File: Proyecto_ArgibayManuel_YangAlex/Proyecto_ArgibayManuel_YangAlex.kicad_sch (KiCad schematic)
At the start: 30 parts, among them J1 Conn_01x02, J2 Conn_01x01, J3 Con_1x2, J4 Con_1x3, J5 Conn_01x03_Pin, J6 Conn_01x07, SW1 SW_Push, SW2 SW_Push, SW3 SW_Push, SW4 SW_Push, U1 PIC18F258-I_SO, U2 HDC2010YPAR, U3 LT1716IS5TRMPBF, U4 LT1716IS5TRMPBF, U5 TXS0108EPW, Y1 Crystal

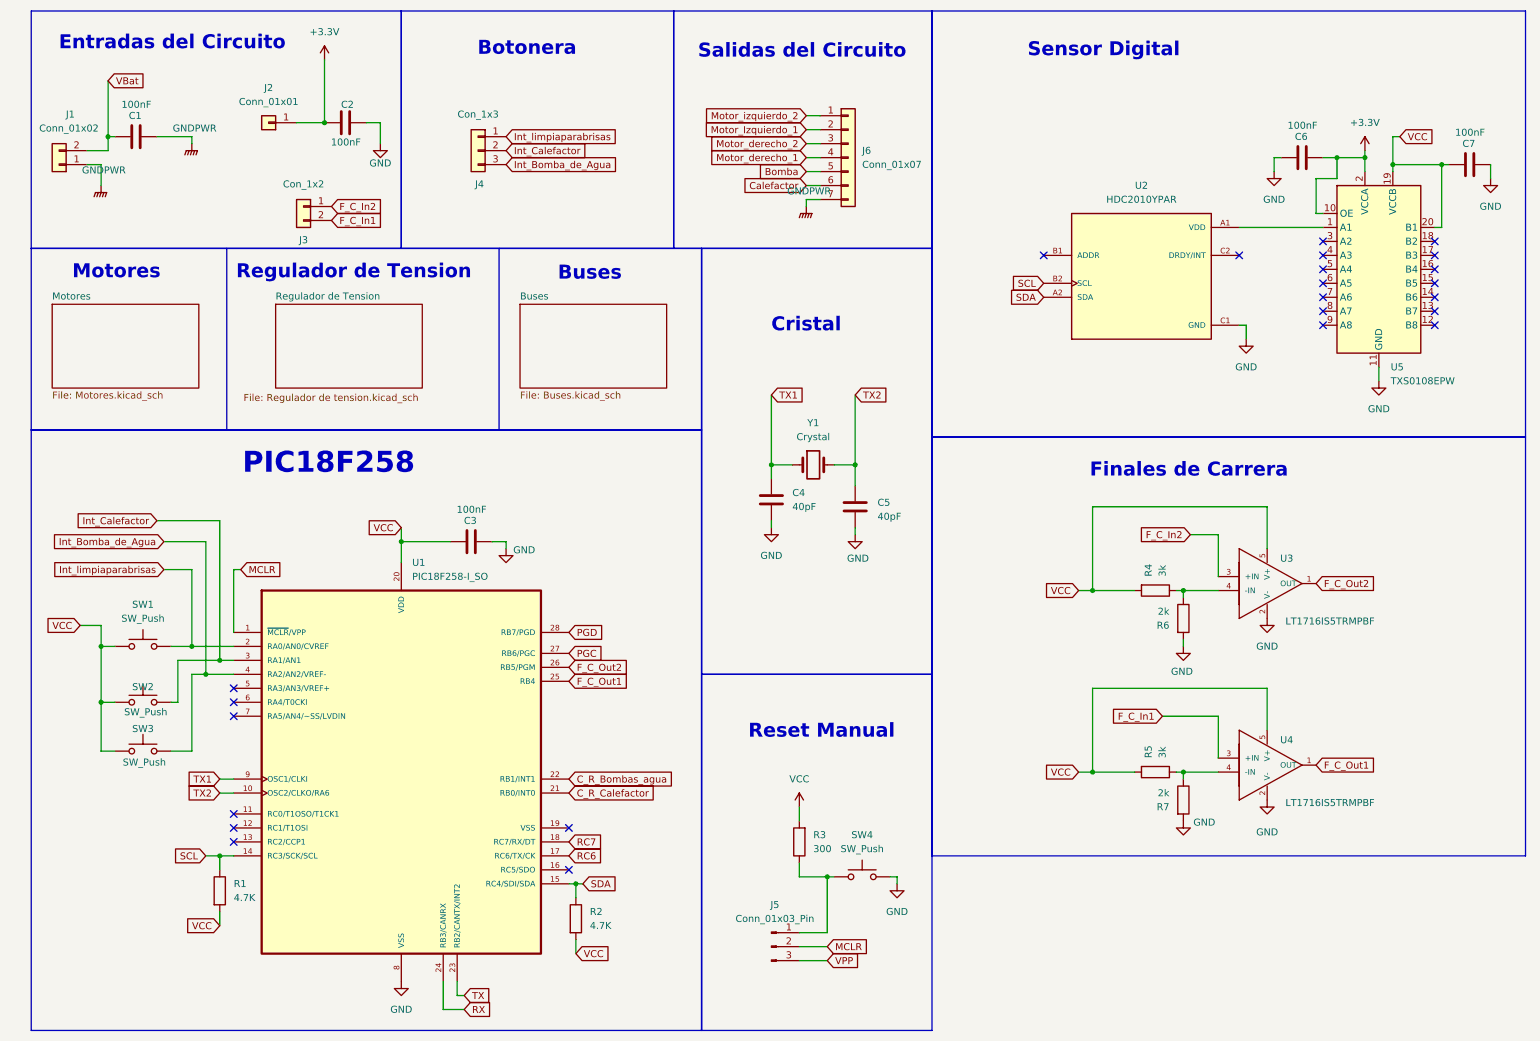
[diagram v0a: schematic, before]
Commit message: Separacion de Botonera
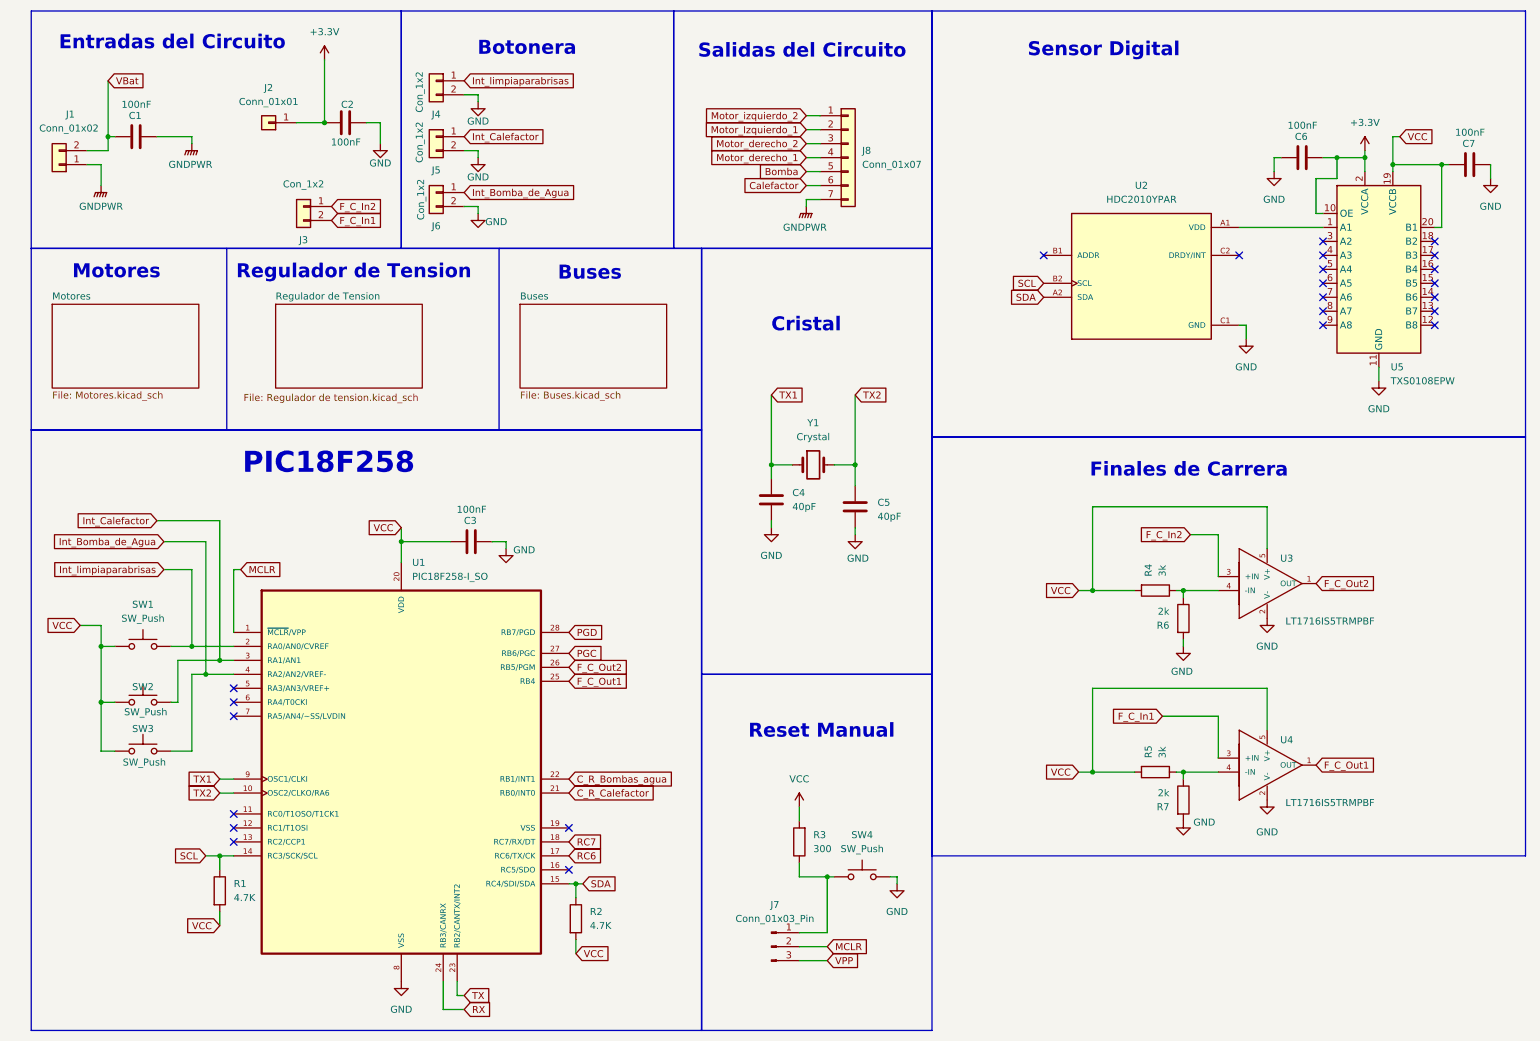
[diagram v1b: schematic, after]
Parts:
- removed J4: Con_1x3, Connector_PinHeader_2.54mm:PinHeader_1x03_P2.54mm_Vertical, symbol Connector_Generic:Conn_01x03
- added J4, J5, J6: Con_1x2, Connector_PinHeader_2.54mm:PinHeader_1x02_P2.54mm_Vertical, symbol Connector_Generic:Conn_01x02
- renumbered J5 to J7, J6 to J8
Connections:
- net GND: now also J4.2 (Pin_2), J5.2 (Pin_2), J6.2 (Pin_2)
- net Int_Bomba_de_Agua: now also J6.1 (Pin_1)
- net Int_Calefactor: now also J5.1 (Pin_1)
- net Int_limpiaparabrisas: now also J4.1 (Pin_1)

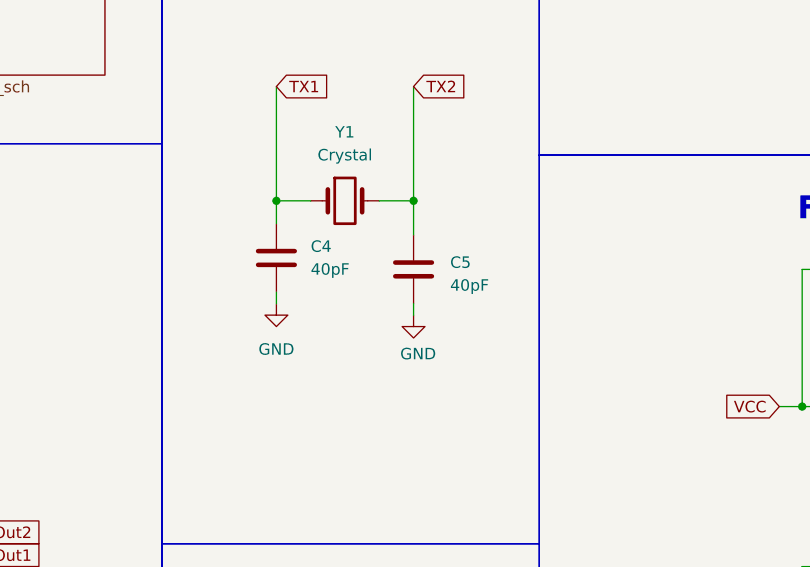
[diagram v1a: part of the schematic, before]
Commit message: cambio de valores de los Condensadores del oscilador
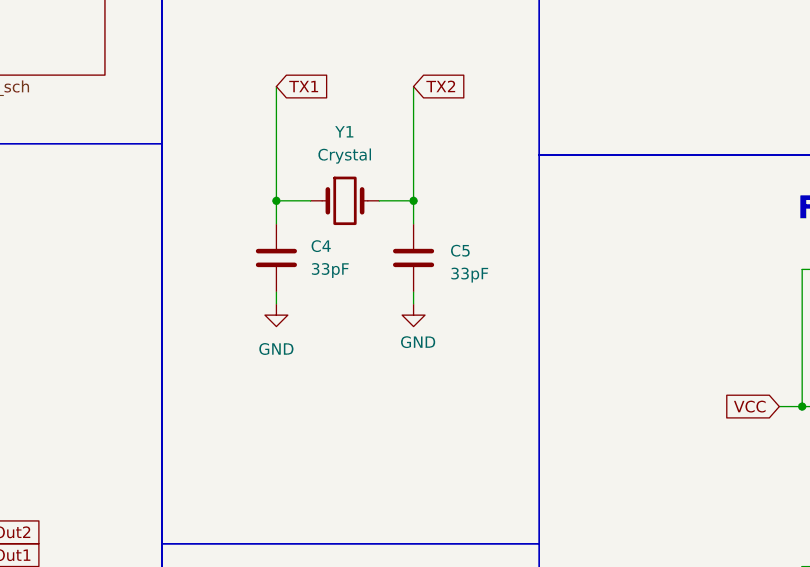
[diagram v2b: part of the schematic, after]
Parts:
- C4, C5: value 40pF -> 33pF
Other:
- moved on the sheet: C5
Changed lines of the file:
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@@
 	(wire
 		(pts
-			(xy 162.56 106.68) (xy 162.56 107.95)
+			(xy 162.56 105.41) (xy 162.56 106.68)
 		)
 		(stroke
@@
 	(wire
 		(pts
-			(xy 162.56 95.25) (xy 162.56 99.06)
+			(xy 162.56 95.25) (xy 162.56 97.79)
 		)
 		(stroke
@@
 	(symbol
 		(lib_id "power:GND")
-		(at 162.56 107.95 0)
+		(at 162.56 106.68 0)
 		(unit 1)
 		(exclude_from_sim no)
@@
 		(dnp no)
 		(property "Reference" "#PWR013"
-			(at 162.56 114.3 0)
+			(at 162.56 113.03 0)
 			(effects
 				(font
@@
 		)
 		(property "Value" "GND"
-			(at 163.068 112.268 0)
+			(at 163.068 110.998 0)
 			(effects
 				(font
@@
 		)
 		(property "Footprint" ""
-			(at 162.56 107.95 0)
+			(at 162.56 106.68 0)
 			(effects
 				(font
@@
 		)
 		(property "Datasheet" ""
-			(at 162.56 107.95 0)
+			(at 162.56 106.68 0)
 			(effects
 				(font
@@
 		)
 		(property "Description" "Power symbol creates a global label with name \"GND\" , ground"
-			(at 162.56 107.95 0)
+			(at 162.56 106.68 0)
 			(effects
 				(font
@@
 	(symbol
 		(lib_id "Device:C")
-		(at 162.56 102.87 0)
+		(at 162.56 101.6 0)
 		(unit 1)
 		(exclude_from_sim no)
@@
 		(dnp no)
 		(property "Reference" "C5"
-			(at 166.624 102.108 0)
+			(at 166.624 100.838 0)
 			(effects
 				(font
@@
 			)
 		)
-		(property "Value" "40pF"
-			(at 166.624 104.648 0)
+		(property "Value" "33pF"
+			(at 166.624 103.378 0)
 			(effects
 				(font
@@
 		)
 		(property "Footprint" "Capacitor_SMD:C_0805_2012Metric"
-			(at 163.5252 106.68 0)
+			(at 163.5252 105.41 0)
 			(effects
 				(font
@@
 		)
 		(property "Datasheet" "~"
-			(at 162.56 102.87 0)
+			(at 162.56 101.6 0)
 			(effects
 				(font
@@
 		)
 		(property "Description" "Unpolarized capacitor"
-			(at 162.56 102.87 0)
+			(at 162.56 101.6 0)
 			(effects
 				(font
@@
 			)
 		)
-		(property "Value" "40pF"
+		(property "Value" "33pF"
 			(at 151.13 102.8699 0)
 			(effects

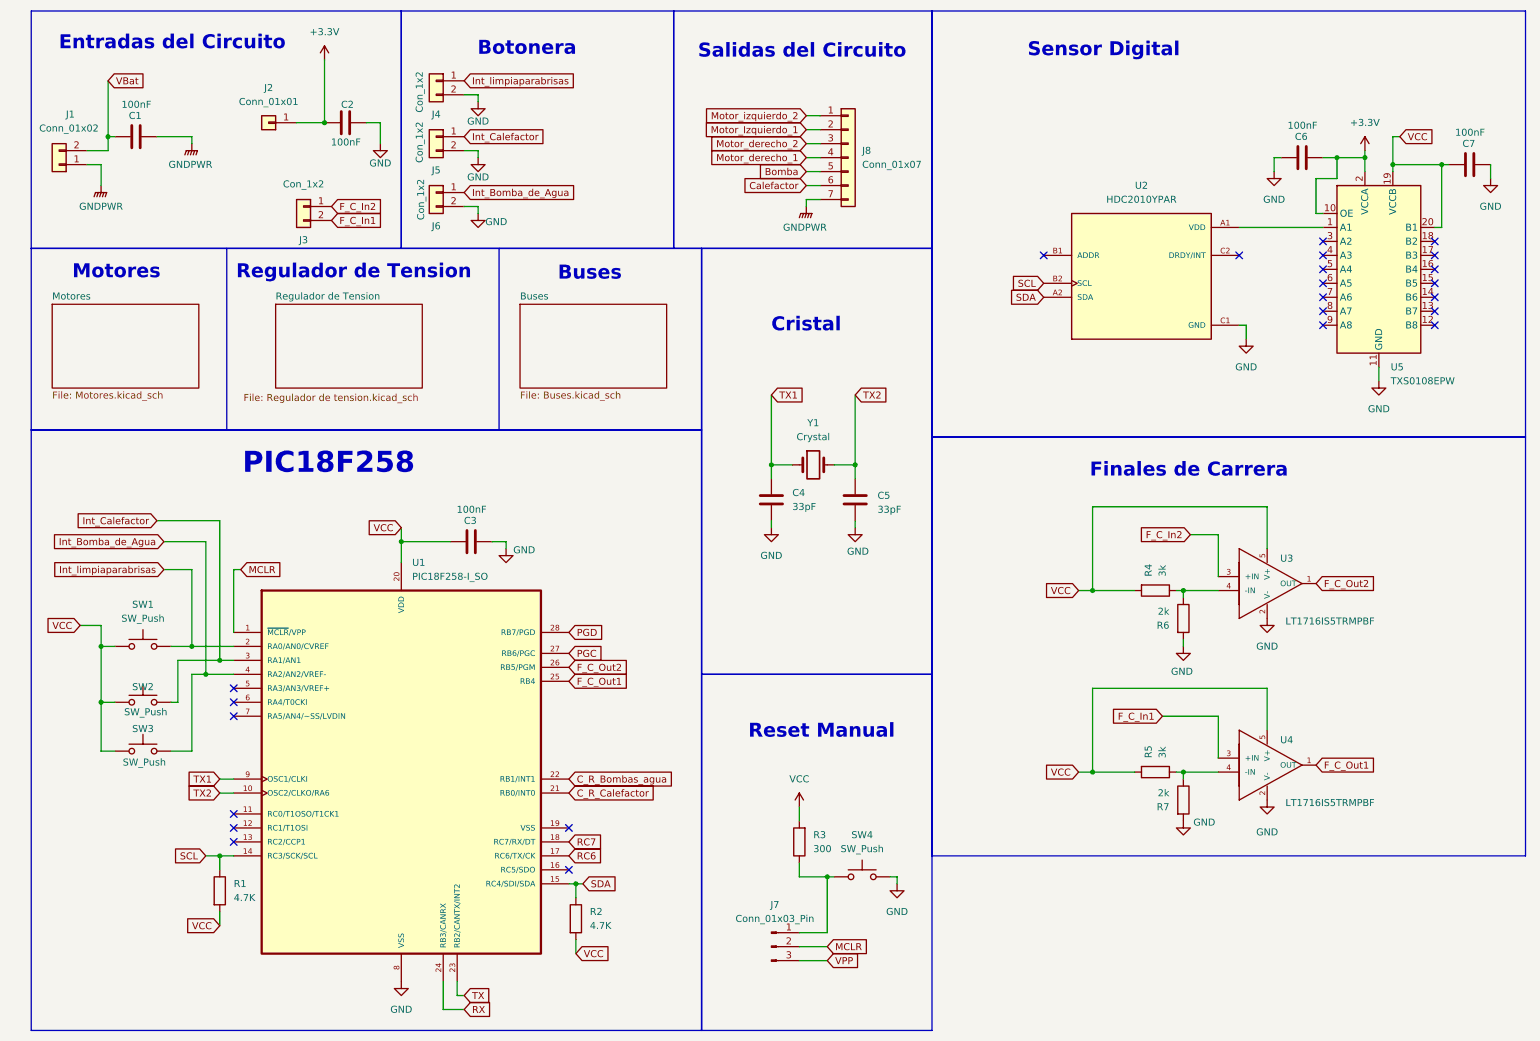
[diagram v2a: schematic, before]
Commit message: cambiar esquematico
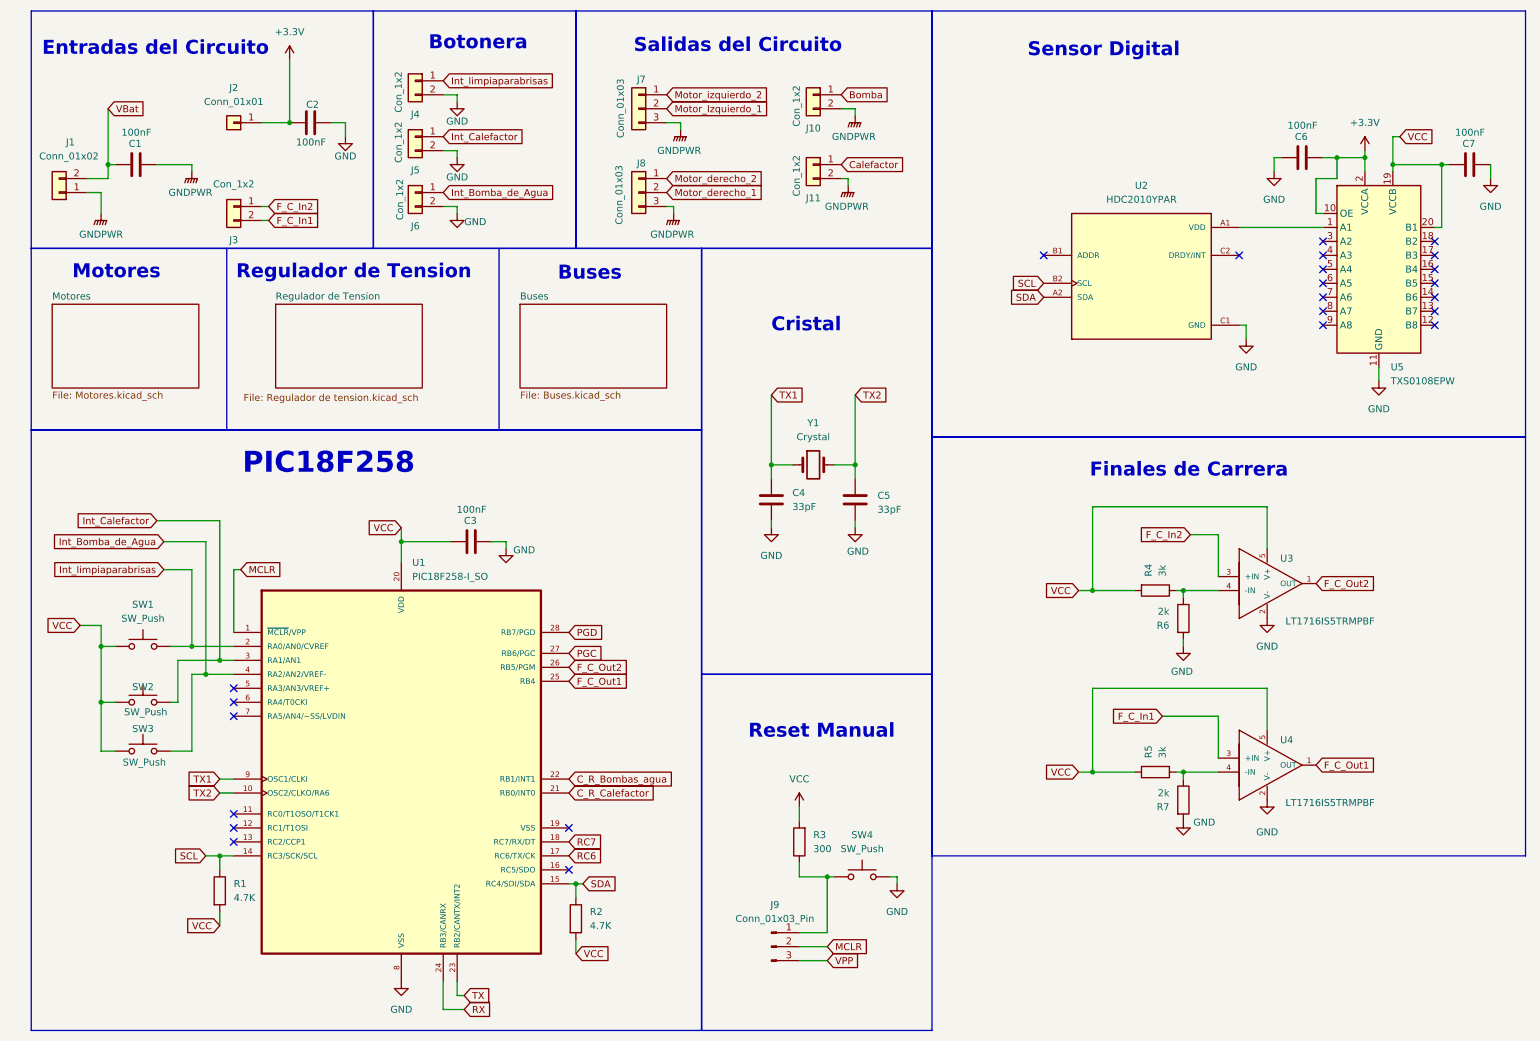
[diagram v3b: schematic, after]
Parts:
- removed J8: Conn_01x07, TerminalBlock_Phoenix:TerminalBlock_Phoenix_MKDS-1,5-7_1x07_P5.00mm_Horizontal, symbol Connector_Generic:Conn_01x07
- added J10, J11: Con_1x2, Connector_PinHeader_2.54mm:PinHeader_1x02_P2.54mm_Vertical, symbol Connector_Generic:Conn_01x02
- added J7, J8: Conn_01x03, Connector_PinHeader_2.54mm:PinHeader_1x03_P2.54mm_Vertical, symbol Connector_Generic:Conn_01x03
- renumbered J7 to J9
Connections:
- net Bomba: now also J10.1 (Pin_1)
- net Calefactor: now also J11.1 (Pin_1)
- net GNDPWR: now also J10.2 (Pin_2), J11.2 (Pin_2), J7.3 (Pin_3), J8.3 (Pin_3)
- net Motor_Izquierdo_1: now also J7.2 (Pin_2)
- net Motor_derecho_1: now also J8.2 (Pin_2)
- net Motor_derecho_2: now also J8.1 (Pin_1)
- net Motor_izquierdo_2: now also J7.1 (Pin_1)
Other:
- moved on the sheet: C1, C2, J1, J2, J3, J4, J5, J6

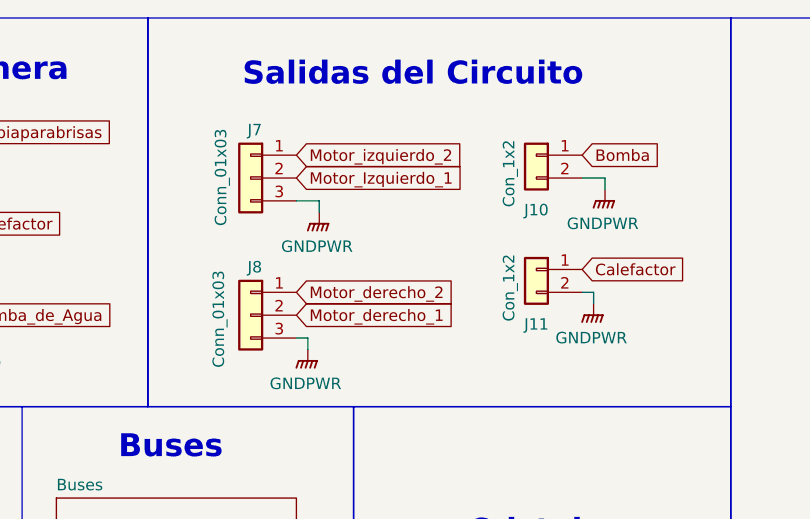
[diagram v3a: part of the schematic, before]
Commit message: Cambio de la PCB(por el cambio de elos conectores)
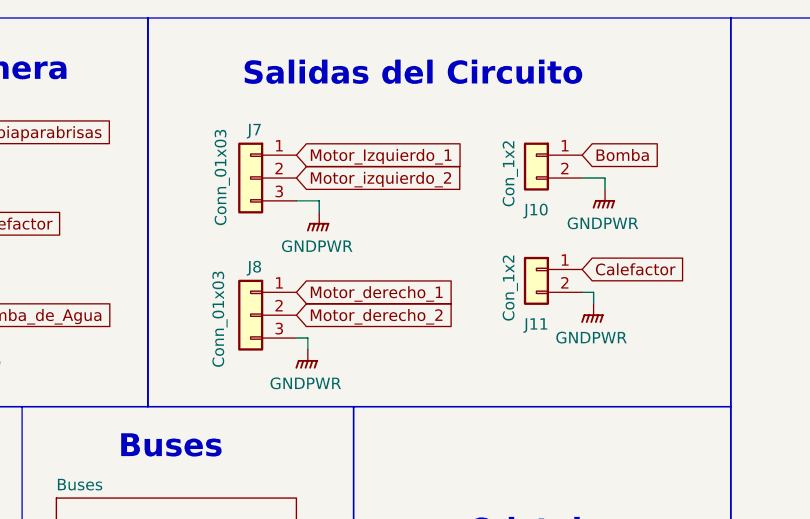
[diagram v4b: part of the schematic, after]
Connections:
- net Motor_Izquierdo_1: now also J7.1 (Pin_1); no longer J7.2 (Pin_2)
- net Motor_derecho_1: now also J8.1 (Pin_1); no longer J8.2 (Pin_2)
- net Motor_derecho_2: now also J8.2 (Pin_2); no longer J8.1 (Pin_1)
- net Motor_izquierdo_2: now also J7.2 (Pin_2); no longer J7.1 (Pin_1)
